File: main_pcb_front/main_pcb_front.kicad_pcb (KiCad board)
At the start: 2 copper layers, 95.6 x 95.6 mm, 12 parts

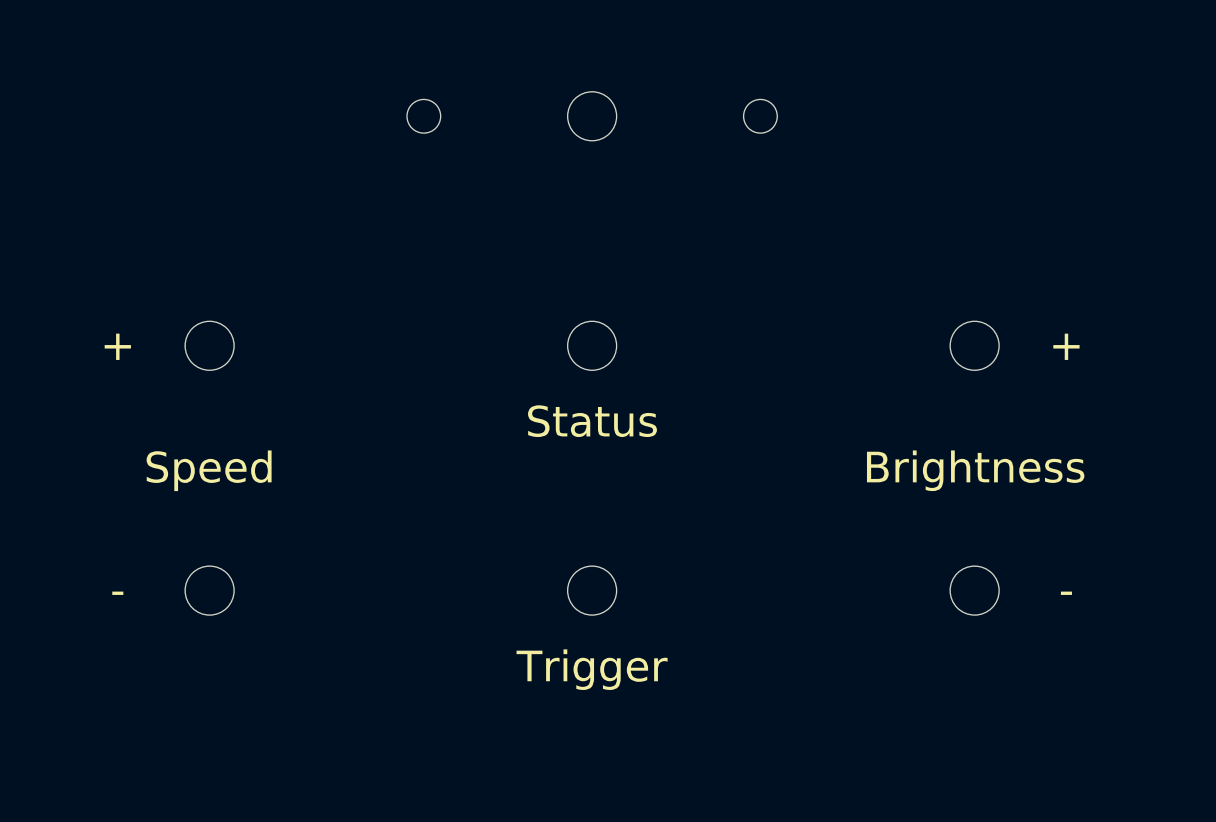
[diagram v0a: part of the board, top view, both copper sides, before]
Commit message: Moved UI to avoid collision with RPi
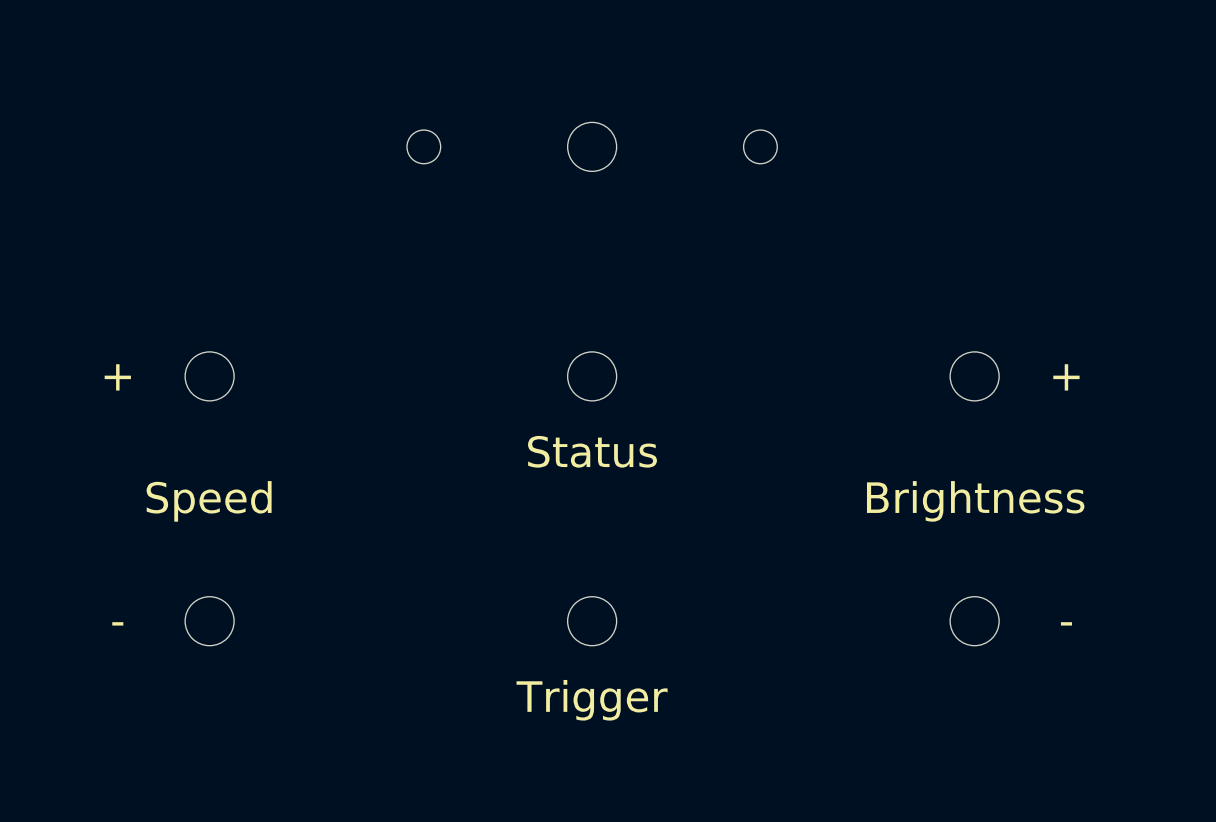
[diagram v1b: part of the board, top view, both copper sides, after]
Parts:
- moved H10 2.00 mm to (173.0, 131.0)
- moved H11 2.00 mm to (148.0, 100.0)
- moved H5 2.00 mm to (123.0, 115.0)
- moved H6 2.00 mm to (123.0, 131.0)
- moved H7 2.00 mm to (148.0, 115.0)
- moved H8 2.00 mm to (148.0, 131.0)
- moved H9 2.00 mm to (173.0, 115.0)

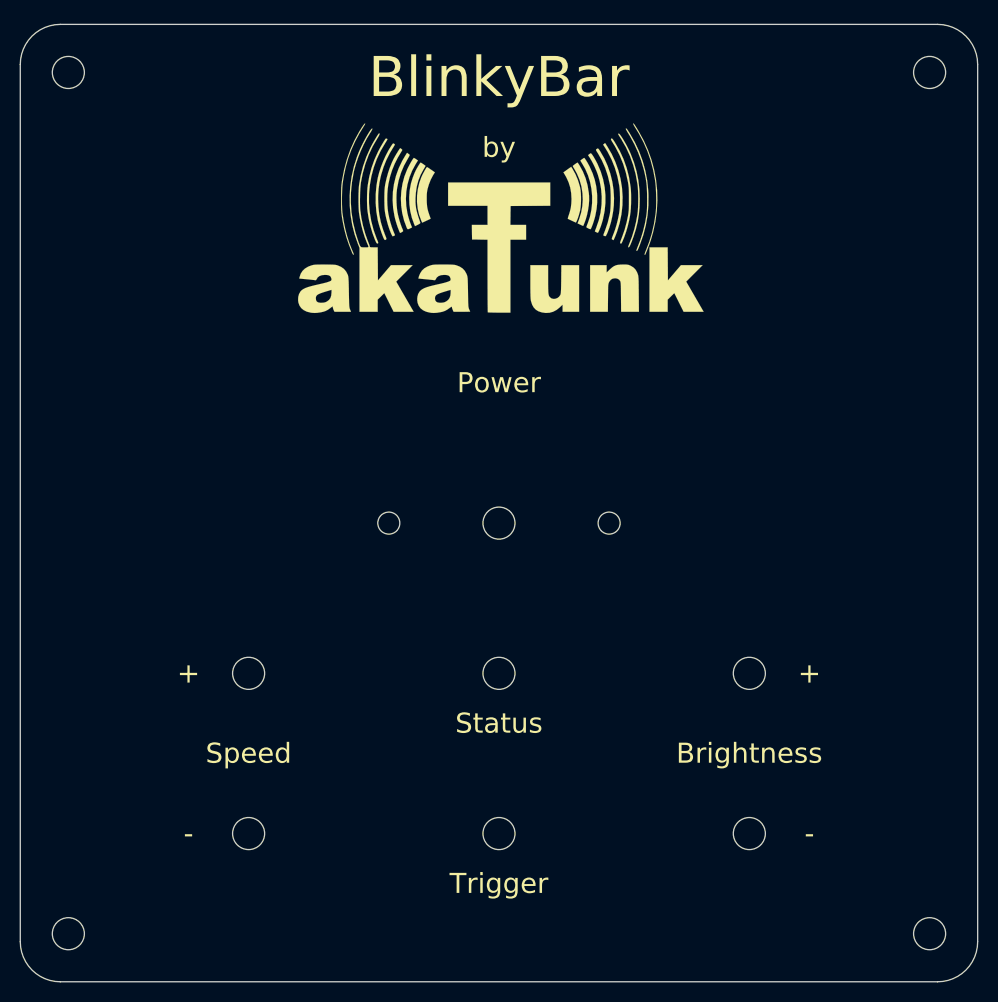
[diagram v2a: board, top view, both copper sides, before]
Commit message: Increased front panel PCB holes for buttons to 4mm
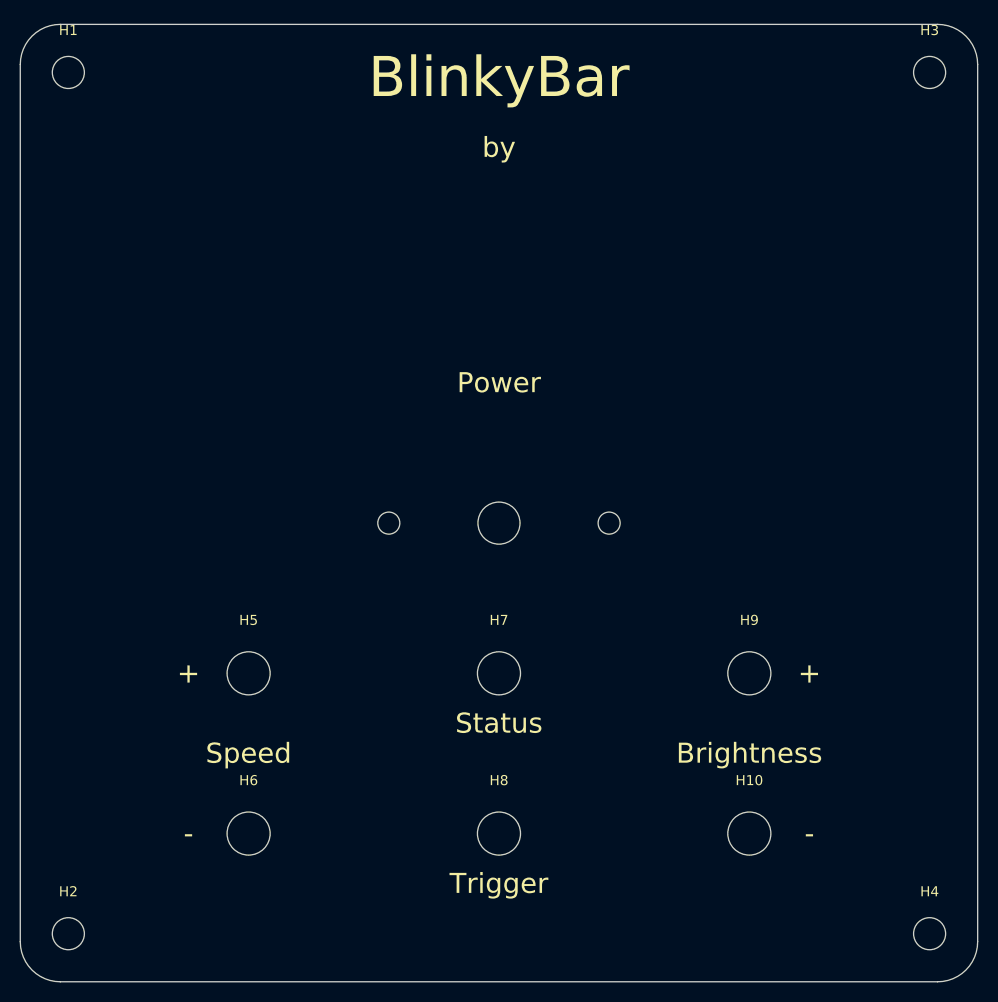
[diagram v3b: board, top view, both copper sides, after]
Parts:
- removed G***: LOGO, akaFunkLogo:akaFunkLogo
- H10, H5, H6, H7, H8, H9: footprint MountingHole:MountingHole_3.2mm_M3 -> MountingHole:MountingHole_4.3mm_M4

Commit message: Merged PCBs to KiCAD 6 format
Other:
- net class Default removed
